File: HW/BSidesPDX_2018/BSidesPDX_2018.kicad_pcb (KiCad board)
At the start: 2 copper layers, 94.7 x 67.7 mm, 4 parts

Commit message: Layout work, added Datasheet for USB connector, fixed OSRAM_LED footprint, Fixed AVR ISP footprint.
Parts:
- removed G*** (x3): LOGO, LOGO
- added ART_Cu: LOGO, BSidesPDX_2018:F_Cu, F.Cu at (148.4, 106.8)
- added BT1: Battery_Cell, BSidesPDX_2018:CR2030_Retainer, B.Cu at (148.4, 132.2)
- added C1: 10u, pkl_dipol:C_0805, B.Cu at (212.1, 89.4)
- added C2: 0.1u, pkl_dipol:C_0402, B.Cu at (207.3, 89.3)
- added D1: YLW_LED, BSidesPDX_2018:OSRAM_LED, F.Cu at (186.9, 167.4)
- added D10: YLW_LED, BSidesPDX_2018:OSRAM_LED, F.Cu at (182.6, 186.2)
- added D101: RGB_LED, BSidesPDX_2018:RGB_LED, F.Cu at (230.5, 179.3)
- added D102: RGB_LED, BSidesPDX_2018:RGB_LED, F.Cu at (229.8, 170.6)
- added D103: RGB_LED, BSidesPDX_2018:RGB_LED, F.Cu at (221.1, 163.3)
- added D104: RGB_LED, BSidesPDX_2018:RGB_LED, F.Cu at (217.6, 173.9)
- added D11: YLW_LED, BSidesPDX_2018:OSRAM_LED, F.Cu at (189.8, 179.6)
- added D12: YLW_LED, BSidesPDX_2018:OSRAM_LED, F.Cu at (199.1, 173.5)
- added D2: YLW_LED, BSidesPDX_2018:OSRAM_LED, F.Cu at (175.3, 180.5)
- added D3: YLW_LED, BSidesPDX_2018:OSRAM_LED, F.Cu at (184.7, 173.5)
- added D4: YLW_LED, BSidesPDX_2018:OSRAM_LED, F.Cu at (194.1, 167.4)
- added D5: YLW_LED, BSidesPDX_2018:OSRAM_LED, F.Cu at (174.6, 187.7)
- added D6: YLW_LED, BSidesPDX_2018:OSRAM_LED, F.Cu at (182.6, 180.1)
- added D7: YLW_LED, BSidesPDX_2018:OSRAM_LED, F.Cu at (191.8, 173.5)
- added D8: YLW_LED, BSidesPDX_2018:OSRAM_LED, F.Cu at (210.8, 152.2)
- added D9: YLW_LED, BSidesPDX_2018:OSRAM_LED, F.Cu at (167.4, 187.7)
- added J1: AVR-ISP-6, BSidesPDX_2018:AVR_ISP_2x3_P2.54mm_SMD, B.Cu at (192.0, 153.0)
- added J2: USB_B_Micro, BSidesPDX_2018:USB_B_Micro, B.Cu at (188.1, 124.2)
- added MASK_ART: LOGO, BSidesPDX_2018:F_Mask, F.Cu at (148.4, 106.8)
- added PDX: LOGO, BSidesPDX_2018:F_Silk, F.Cu at (148.4, 106.8)
- added R1: 100R, pkl_dipol:R_0603, B.Cu at (222.0, 86.7)
- added R101: 100R, pkl_dipol:R_0603, B.Cu at (234.2, 99.8)
- added R102: 100R, pkl_dipol:R_0603, B.Cu at (229.6, 99.6)
- added R103: 100R, pkl_dipol:R_0603, B.Cu at (224.6, 100.1)
- added R104: 100R, pkl_dipol:R_0603, B.Cu at (238.5, 99.9)
- added R2: 100R, pkl_dipol:R_0603, B.Cu at (224.4, 86.7)
- added R3: 100R, pkl_dipol:R_0603, B.Cu at (226.8, 86.7)
- added R4: 100R, pkl_dipol:R_0603, B.Cu at (215.8, 94.9)
- added R5: 51R, pkl_dipol:R_0603, B.Cu at (184.8, 130.8)
- added R6: 51R, pkl_dipol:R_0603, B.Cu at (181.4, 130.8)
- added R7: 1K, pkl_dipol:R_0603, B.Cu at (177.8, 133.1)
- added S1: PTS645SM43SMTR92_LFS, digikey-footprints:Switch_Tactile_SMD_6x6mm_PTS645, B.Cu at (129.4, 150.2)
- added S2: PTS645SM43SMTR92_LFS, digikey-footprints:Switch_Tactile_SMD_6x6mm_PTS645, B.Cu at (160.2, 150.9)
- added U1: ATTINY861-15XD, Package_SO:TSSOP-20_4.4x6.5mm_P0.65mm, B.Cu at (125.5, 173.3)
- added X1: Badgelife_shitty_connector, BSidesPDX_2018:PRESS_FIT_SAO_CNX, F.Cu at (113.3, 81.7)
- added X2: Badgelife_shitty_connector, BSidesPDX_2018:PRESS_FIT_SAO_CNX, F.Cu at (183.3, 81.7)
- added X3: Badgelife_shitty_connector, BSidesPDX_2018:PRESS_FIT_SAO_CNX, F.Cu at (113.3, 135.2)
- added X4: Badgelife_shitty_connector, BSidesPDX_2018:PRESS_FIT_SAO_CNX, F.Cu at (183.3, 135.2)
- moved ? 182.8 mm to (148.4, 87.4)

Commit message: added OSHPark art, placed parts
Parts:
- moved D101 121.6 mm to (130.0, 110.8)
- moved D12 107.8 mm to (127.1, 93.3)
- moved D11 106.4 mm to (136.9, 87.2)
- moved D10 104.0 mm to (120.5, 102.7)
- moved D102 100.6 mm to (145.0, 116.4)
- moved D8 94.0 mm to (120.6, 125.6)
- moved D9 88.2 mm to (118.4, 114.3)
- moved D2 87.1 mm to (169.6, 93.6)
- moved D1 85.1 mm to (159.8, 86.8)
- moved D103 81.8 mm to (154.1, 116.3)
- moved D104 79.2 mm to (163.3, 116.3)
- moved U1 75.4 mm to (148.5, 101.4)
- moved D7 75.1 mm to (127.2, 135.3)
- moved D3 71.3 mm to (176.0, 102.7)
- moved D5 62.2 mm to (176.1, 125.5)
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
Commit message: changed library settings, changed charliplexing circuit, fixed USB resistor
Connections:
- D1 pad 1: /ROW2 -> /ROW_2
- D10 pad 1: /ROW2 -> /ROW_2
- D11 pad 1: /ROW3 -> /ROW_3
- D12 pad 1: /ROW4 -> /ROW_4
- D2 pad 1: /ROW3 -> /ROW_3
- D3 pad 1: /ROW4 -> /ROW_4
- D4 pad 1: /ROW1 -> /ROW_1
- D5 pad 1: /ROW3 -> /ROW_3
- D6 pad 1: /ROW4 -> /ROW_4
- D7 pad 1: /ROW1 -> /ROW_1
- D8 pad 1: /ROW1 -> /ROW_1
- D9 pad 1: /ROW2 -> /ROW_2
- R7 pad 2: /SCL_SCK_D- -> /D-

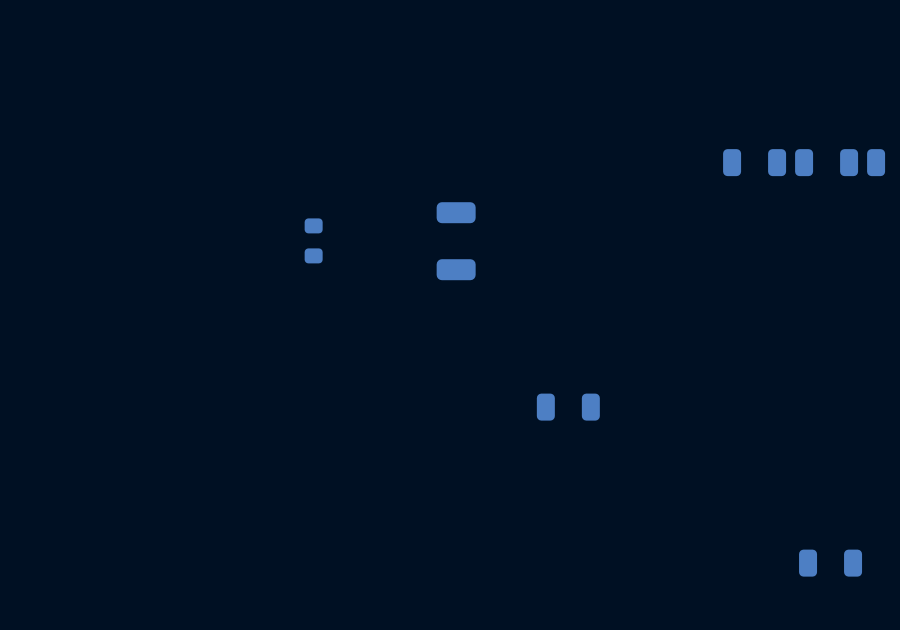
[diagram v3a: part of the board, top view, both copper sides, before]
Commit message: Moved foot prints from libraries to locally.
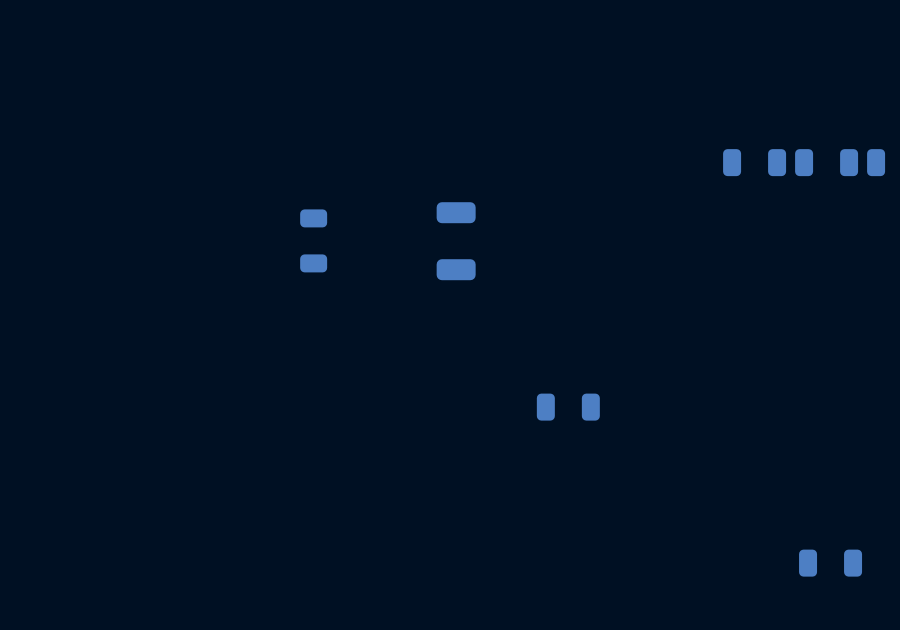
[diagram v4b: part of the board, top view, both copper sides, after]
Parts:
- C1: footprint pkl_dipol:C_0805 -> BSidesPDX_2018:C_0805
- C2: footprint pkl_dipol:C_0402 -> BSidesPDX_2018:C_0603
- R1, R101, R102, R103, R104, R2, R3, R4, R5, R6, R7: footprint pkl_dipol:R_0603 -> BSidesPDX_2018:C_0603
- S1, S2: footprint digikey-footprints:Switch_Tactile_SMD_6x6mm_PTS645 -> BSidesPDX_2018:Switch_Tactile_SMD_6x6mm_PTS645
- turned R4 to 180 degrees

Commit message: fixed avr isp orientation
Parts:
- J1: moved to F.Cu
- moved U1 3.20 mm to (148.8, 98.2), turned to 0 degrees
- turned J1 to 0 degrees

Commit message: adding Joe's layout
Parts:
- moved R101 99.6 mm to (135.1, 110.1), turned to 180 degrees
- moved J1 94.4 mm to (141.6, 98.8), turned to 180 degrees
- moved R102 81.3 mm to (149.1, 111.1), turned to 270 degrees
- moved R104 74.9 mm to (164.5, 111.2), turned to 270 degrees
- moved R103 68.8 mm to (156.7, 111.1), turned to 270 degrees
- moved R3 66.2 mm to (161.2, 95.1)
- moved R1 65.5 mm to (156.9, 92.9), turned to 180 degrees
- moved R2 62.8 mm to (161.9, 92.8)
- moved C1 61.5 mm to (151.9, 102.0), turned to 90 degrees
- moved D3 59.9 mm to (120.7, 125.7)
- moved D9 58.8 mm to (176.1, 125.8)
- moved D12 55.4 mm to (178.4, 114.3), turned to 180 degrees
- moved D4 55.3 mm to (127.1, 93.1), turned to 180 degrees
- moved C2 54.9 mm to (153.9, 102.0), turned to 90 degrees
- moved R4 54.8 mm to (161.1, 97.3), turned to 0 degrees
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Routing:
- net /SDA_MOSI_D+: track 0.00 -> 247.5 mm, vias 0 -> 3
- net /SCL_SCK_D-: track 0.00 -> 246.9 mm, vias 0 -> 3
- net /ROW_2: track 0.00 -> 109.4 mm
- net /ROW_3: track 0.00 -> 102.1 mm
- net /ROW_4: track 0.00 -> 101.7 mm
- net /ROW_1: track 0.00 -> 92.3 mm, vias 0 -> 2
- net /L_SWITCH: track 0.00 -> 91.0 mm, vias 0 -> 4
- net /R_PWM__MISO: track 0.00 -> 75.2 mm, vias 0 -> 2
- net /G_PWM: track 0.00 -> 62.2 mm, vias 0 -> 6
- net /B_PWM: track 0.00 -> 59.0 mm, vias 0 -> 2
- net /R_SWITCH: track 0.00 -> 37.9 mm, vias 0 -> 2
- net /~RESET: track 0.00 -> 27.8 mm, vias 0 -> 2
- net /EN_RGB1: track 0.00 -> 24.8 mm
- net /3V0: track 0.00 -> 13.5 mm, vias 0 -> 2
- net /EN_RGB4: track 0.00 -> 11.7 mm
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- added copper zone on B.Cu, net GND

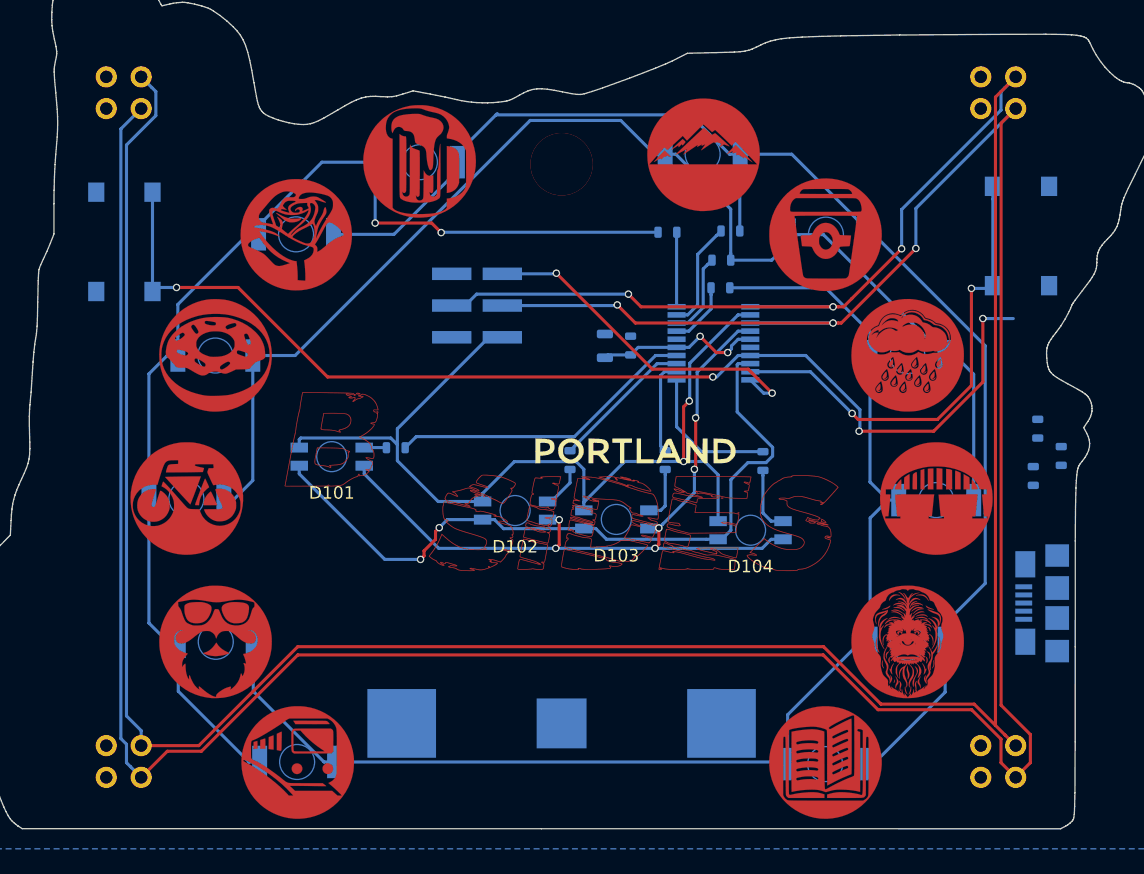
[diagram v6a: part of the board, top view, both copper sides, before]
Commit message: power mostly routed, most signals routed
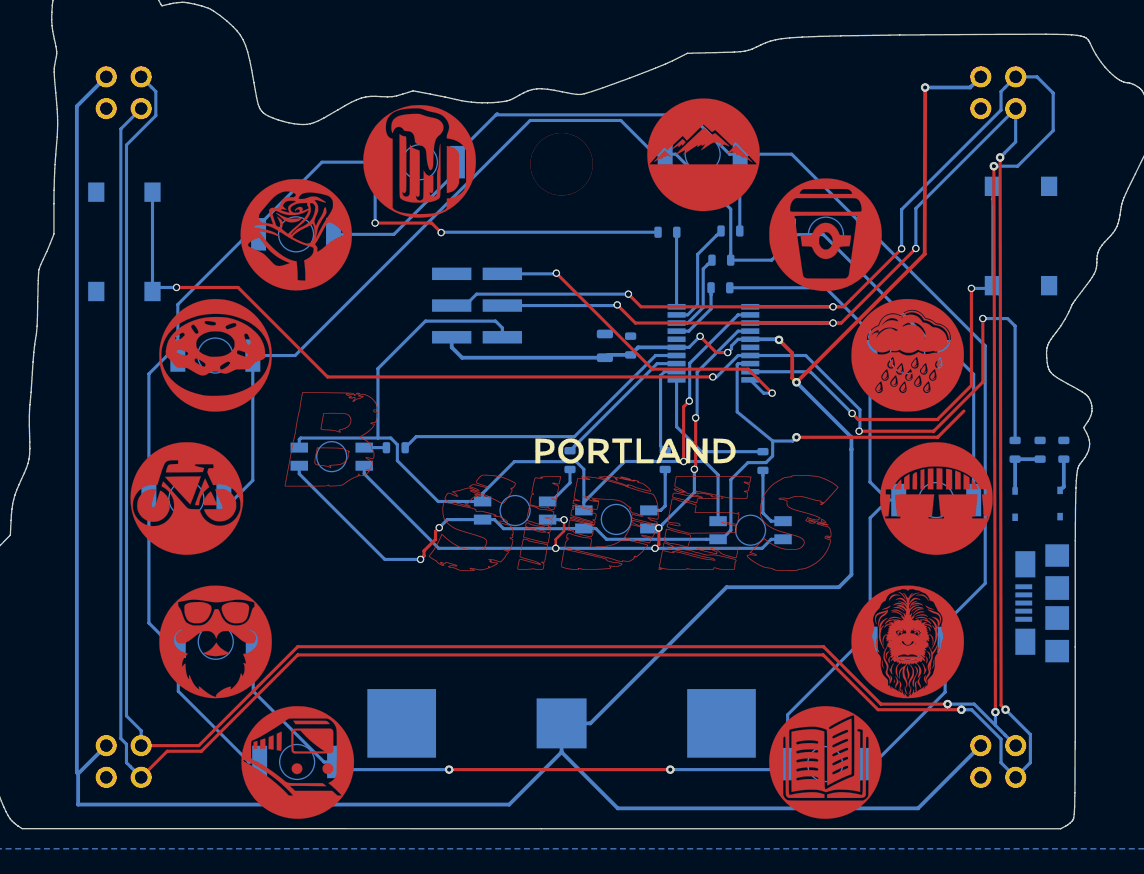
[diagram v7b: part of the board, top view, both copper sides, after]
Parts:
- added D13: D_Zener, Diode_SMD:D_SOD-323, B.Cu at (188.3, 114.6)
- added D14: D_Zener, Diode_SMD:D_SOD-323, B.Cu at (184.7, 114.7)
- moved R6 2.55 mm to (184.7, 110.3), turned to 90 degrees
- moved R7 1.70 mm to (186.7, 110.3), turned to 270 degrees
- moved R5 0.54 mm to (188.6, 110.3), turned to 270 degrees
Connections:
- D101 pad 4: /B_PWM -> /B_PWM__D+
- D102 pad 4: /B_PWM -> /B_PWM__D+
- D103 pad 4: /B_PWM -> /B_PWM__D+
- D104 pad 4: /B_PWM -> /B_PWM__D+
- J1 pad 3: /SCL_SCK_D- -> /SCL_SCK
- J1 pad 4: /SDA_MOSI_D+ -> /SDA_MOSI
- R5 pad 1: /SDA_MOSI_D+ -> /B_PWM__D+
- R6 pad 2: /SCL_SCK_D- -> /L_SWITCH_D-
- S1 pad 1: /L_SWITCH -> /L_SWITCH_D-
- S1 pad 2: /L_SWITCH -> /L_SWITCH_D-
- U1 pad 1: /SDA_MOSI_D+ -> /SDA_MOSI
- U1 pad 3: /SCL_SCK_D- -> /SCL_SCK
- U1 pad 7: /L_SWITCH -> /L_SWITCH_D-
- U1 pad 8: /B_PWM -> /B_PWM__D+
- X1 pad 3: /SCL_SCK_D- -> /SCL_SCK
- X1 pad 4: /SDA_MOSI_D+ -> /SDA_MOSI
- X2 pad 3: /SCL_SCK_D- -> /SCL_SCK
- X2 pad 4: /SDA_MOSI_D+ -> /SDA_MOSI
- X3 pad 3: /SCL_SCK_D- -> /SCL_SCK
- X3 pad 4: /SDA_MOSI_D+ -> /SDA_MOSI
- X4 pad 3: /SCL_SCK_D- -> /SCL_SCK
- X4 pad 4: /SDA_MOSI_D+ -> /SDA_MOSI
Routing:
- net /SDA_MOSI: track 0.00 -> 252.2 mm, vias 0 -> 6
- net /SDA_MOSI_D+: track 247.5 -> 0.00 mm, vias 3 -> 0
- net /SCL_SCK: track 0.00 -> 246.9 mm, vias 0 -> 6
- net /SCL_SCK_D-: track 246.9 -> 0.00 mm, vias 3 -> 0
- net /3V0: track 13.5 -> 254.0 mm, vias 2 -> 5
- net /L_SWITCH_D-: track 0.00 -> 100.5 mm, vias 0 -> 4
- net /L_SWITCH: track 91.0 -> 0.00 mm, vias 4 -> 0
- net /B_PWM__D+: track 0.00 -> 75.4 mm, vias 0 -> 3
- net /B_PWM: track 59.0 -> 0.00 mm, vias 2 -> 0
- net /R_PWM__MISO: track 75.2 -> 80.6 mm
- net /D-: track 0.00 -> 4.55 mm
- net /D+: track 0.00 -> 2.62 mm
- net /G_PWM: track 62.2 -> 62.8 mm
- net /ROW_4: vias 0 -> 2
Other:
- net class Default: clearance 0.2 -> 0.254; trace_width 0.25 -> 0.254; via_dia 0.6 -> 0.6858; via_drill 0.4 -> 0.3302
- rule trace_clearance: 0.2 -> 0.254
- rule trace_min: 0.2 -> 0.1524
- rule via_min_drill: 0.3 -> 0.3302
- rule via_min_size: 0.4 -> 0.6858

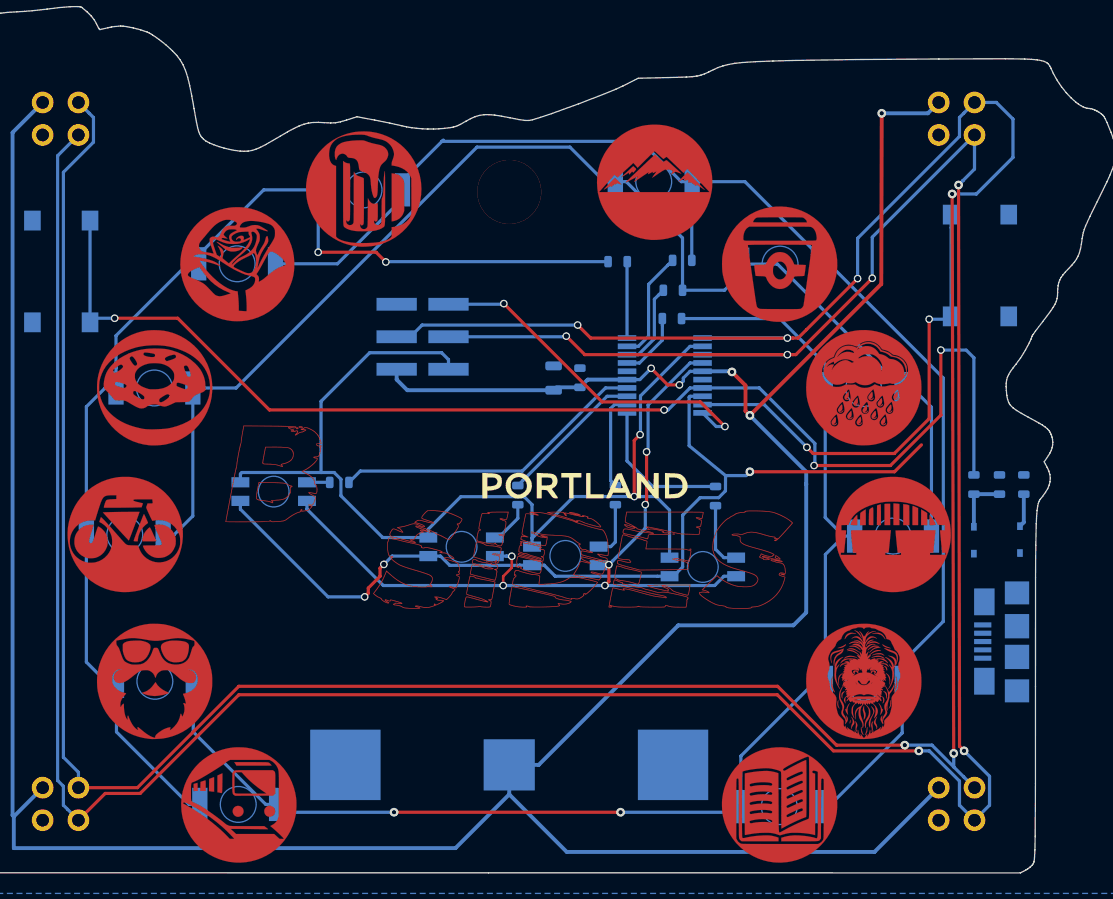
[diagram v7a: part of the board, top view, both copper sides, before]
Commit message: layout done, FAILS DRC
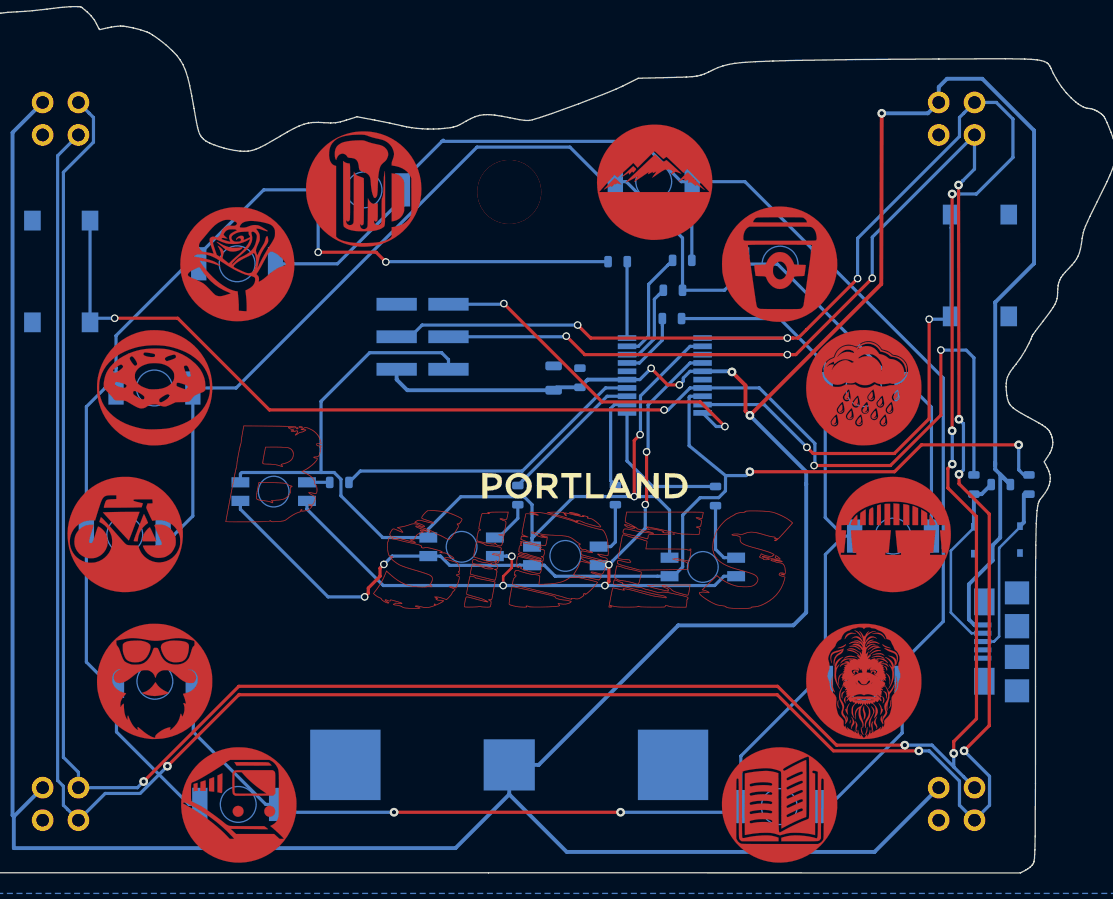
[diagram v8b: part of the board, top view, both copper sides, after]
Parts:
- moved R5 0.40 mm to (189.0, 110.3)
- moved R7 0.10 mm to (186.8, 110.3), turned to 180 degrees
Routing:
- net /3V0: track 254.0 -> 309.0 mm
- net /D+: track 2.62 -> 13.4 mm
- net /D-: track 4.55 -> 14.8 mm
- net /B_PWM__D+: track 75.4 -> 85.6 mm, vias 3 -> 4
- net /SCL_SCK: track 246.9 -> 248.9 mm, vias 6 -> 9
- net /SDA_MOSI: track 252.2 -> 254.0 mm, vias 6 -> 9
